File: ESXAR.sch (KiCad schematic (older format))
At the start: 43 parts, among them P1 ANALOG, P10 USB_A, P11 USB_B, P12 SERVO/INPUT, P13 ANALOG, P16 BREADBOARD_POWER, P17 SENSOR, P18 EXTIO, P19 UNIVERSAL, P2 BREADBOARD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

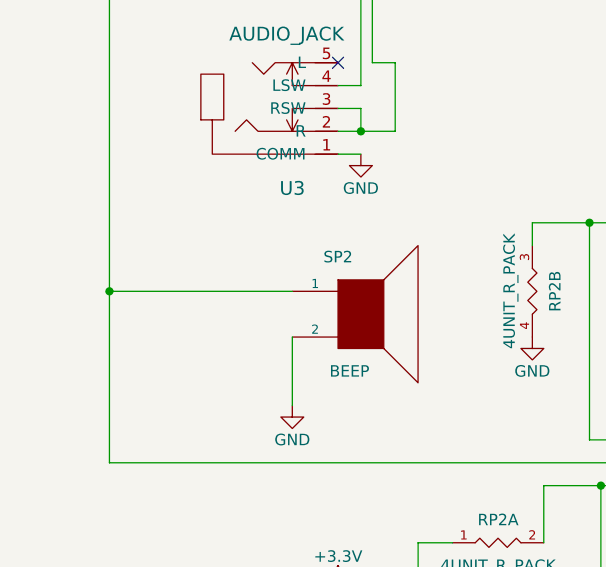
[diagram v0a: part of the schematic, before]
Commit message: Change IO Ext pin direction, and througehwole size.
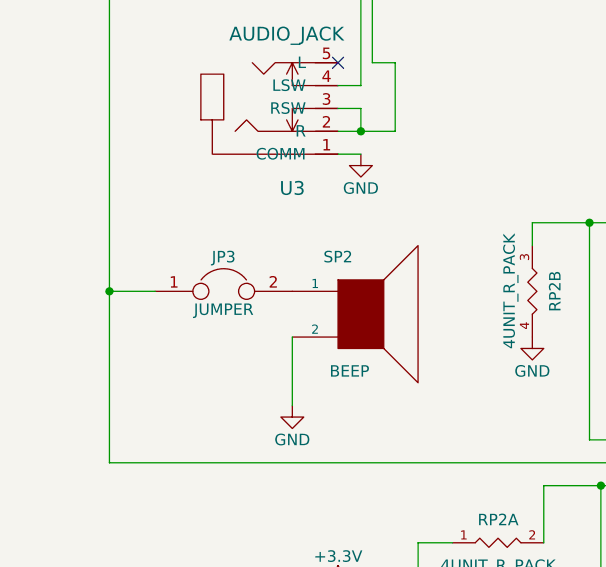
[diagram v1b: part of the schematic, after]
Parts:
- added JP3: JUMPER, symbol JUMPER
- P18, P19, P20: footprint library:SolderWirePad_Oval_9xInline_0-6mmDrill -> library:SolderWirePad_Oval_9xInline_0-7mmDrill
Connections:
- net at P18.7 (P7), P2.7 (P7), P5.7 (P7)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: now also JP3.1; no longer SP2.1
- new net: JP3.2, SP2.1
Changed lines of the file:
@@
 F 0 "P18" H 7900 6200 50  0000 C CNN
 F 1 "EXTIO" H 7900 6300 50  0000 C CNN
-F 2 "library:SolderWirePad_Oval_9xInline_0-6mmDrill" H 7900 5700 50  0001 C CNN
+F 2 "library:SolderWirePad_Oval_9xInline_0-7mmDrill" H 7900 5700 50  0001 C CNN
 F 3 "" H 7900 5700 50  0000 C CNN
 	1    7900 5700
@@
 F 0 "P19" H 9350 6200 50  0000 C CNN
 F 1 "UNIVERSAL" H 9350 6300 50  0000 C CNN
-F 2 "library:SolderWirePad_Oval_9xInline_0-6mmDrill" H 9350 5700 50  0001 C CNN
+F 2 "library:SolderWirePad_Oval_9xInline_0-7mmDrill" H 9350 5700 50  0001 C CNN
 F 3 "" H 9350 5700 50  0000 C CNN
 	1    9350 5700
@@
 F 0 "P20" H 9650 6200 50  0000 C CNN
 F 1 "UNIVERSAL" H 9800 6300 50  0000 C CNN
-F 2 "library:SolderWirePad_Oval_9xInline_0-6mmDrill" H 9650 5700 50  0001 C CNN
+F 2 "library:SolderWirePad_Oval_9xInline_0-7mmDrill" H 9650 5700 50  0001 C CNN
 F 3 "" H 9650 5700 50  0000 C CNN
 	1    9650 5700
@@
 Wire Wire Line
 	2200 5250 2200 4950
-Wire Wire Line
-	2200 4750 1400 4750
 Connection ~ 1400 4750
 Wire Wire Line
@@
 Wire Wire Line
 	2550 3750 2650 3750
+$Comp
+L JUMPER JP3
+U 1 1 57A07E84
+P 1900 4750
+F 0 "JP3" H 1900 4900 50  0000 C CNN
+F 1 "JUMPER" H 1900 4670 50  0000 C CNN
+F 2 "" H 1900 4750 50  0001 C CNN
+F 3 "" H 1900 4750 50  0000 C CNN
+	1    1900 4750
+	1    0    0    -1
+$EndComp
+Wire Wire Line
+	1400 4750 1600 4750
 $EndSCHEMATC

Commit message: fix registor array bug
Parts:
- RP2: footprint Resistors_SMD:R_Array_Convex_4x1206 -> library:R_Array_For_R_Multi_library_4x1206
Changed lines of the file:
@@
 F 0 "RP2" H 3250 4850 50  0000 C CNN
 F 1 "4UNIT_R_PACK" H 3250 4650 50  0000 C CNN
-F 2 "Resistors_SMD:R_Array_Convex_4x1206" H 3200 4650 50  0001 C CNN
+F 2 "library:R_Array_For_R_Multi_library_4x1206" H 3200 4650 50  0001 C CNN
 F 3 "" H 3200 4650 50  0000 C CNN
 	2    3250 4750
@@
 F 0 "RP2" H 3850 3700 50  0000 C CNN
 F 1 "4UNIT_R_PACK" H 3850 3500 50  0000 C CNN
-F 2 "Resistors_SMD:R_Array_Convex_4x1206" H 3800 3500 50  0001 C CNN
+F 2 "library:R_Array_For_R_Multi_library_4x1206" H 3800 3500 50  0001 C CNN
 F 3 "" H 3800 3500 50  0000 C CNN
 	3    3850 3600
@@
 F 0 "RP2" H 3100 5950 50  0000 C CNN
 F 1 "4UNIT_R_PACK" H 3100 5750 50  0000 C CNN
-F 2 "Resistors_SMD:R_Array_Convex_4x1206" H 3050 5750 50  0001 C CNN
+F 2 "library:R_Array_For_R_Multi_library_4x1206" H 3050 5750 50  0001 C CNN
 F 3 "" H 3050 5750 50  0000 C CNN
 	1    3100 5850
@@
 F 0 "RP2" H 6150 3550 50  0000 C CNN
 F 1 "4UNIT_R_PACK" H 6150 3350 50  0000 C CNN
-F 2 "Resistors_SMD:R_Array_Convex_4x1206" H 6100 3350 50  0001 C CNN
+F 2 "library:R_Array_For_R_Multi_library_4x1206" H 6100 3350 50  0001 C CNN
 F 3 "" H 6100 3350 50  0000 C CNN
 	4    6150 3450

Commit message: Ver 20160802. add speaker jumper,change analog port layout, etc.
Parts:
- added R1: 4.7kΩ, Resistors_SMD:R_1206, symbol R
- JP3: footprint (none) -> Pin_Headers:Pin_Header_Straight_1x02
- U5: footprint Housings_DIP:DIP-4_W7.62mm -> Opto-Devices:Optocoupler_SMD_HandSoldering_KPC357_LTV35x_PC357_SingleChannel
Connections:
- net GND: now also R1.1
- net at P13.1 (P1), P17.2 (P2), P8.2 (P2)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: now also R1.2
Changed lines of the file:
@@
 F 0 "U5" H 7150 2900 50  0000 L CNN
 F 1 "TLP222A" H 7350 2900 50  0000 L CNN
-F 2 "Housings_DIP:DIP-4_W7.62mm" H 7150 2500 50  0000 L CIN
+F 2 "Opto-Devices:Optocoupler_SMD_HandSoldering_KPC357_LTV35x_PC357_SingleChannel" H 7150 2500 50  0000 L CIN
 F 3 "" H 7300 2700 50  0000 L CNN
 	1    7350 2700
@@
 	5150 3300 5150 3150
 Wire Wire Line
-	4900 3300 5150 3300
+	4750 3300 5150 3300
 Wire Wire Line
 	4900 3250 4900 3300
@@
 F 0 "JP3" H 1900 4900 50  0000 C CNN
 F 1 "JUMPER" H 1900 4670 50  0000 C CNN
-F 2 "" H 1900 4750 50  0001 C CNN
+F 2 "Pin_Headers:Pin_Header_Straight_1x02" H 1900 4750 50  0001 C CNN
 F 3 "" H 1900 4750 50  0000 C CNN
 	1    1900 4750
@@
 Wire Wire Line
 	1400 4750 1600 4750
+$Comp
+L R R1
+U 1 1 57A07626
+P 4750 3100
+F 0 "R1" V 4830 3100 50  0000 C CNN
+F 1 "4.7kΩ" V 4750 3100 50  0000 C CNN
+F 2 "Resistors_SMD:R_1206" V 4680 3100 50  0001 C CNN
+F 3 "" H 4750 3100 50  0000 C CNN
+	1    4750 3100
+	-1   0    0    1
+$EndComp
+Wire Wire Line
+	4750 3250 4750 3300
+Connection ~ 4900 3300
+Connection ~ 4750 2950
 $EndSCHEMATC

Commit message: Ver 20160804 Layout Change.
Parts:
- added C5, C8: 100uF, Capacitors_ThroughHole:C_Radial_D6.3_L11.2_P2.5, symbol CP
- added C6, C7: 10uF, library:C_1206_HandSoldering_Small, symbol C
- added L1: 4.7uH, library:C_1206_HandSoldering_Small, symbol INDUCTOR_SMALL
- added SW2: DIN, Buttons_Switches_ThroughHole:SW_PUSH_SMALL, symbol SW_PUSH
- added U4: MT5201-3.3N, TO_SOT_Packages_SMD:SOT-23-5, symbol MT5201-3.3N
- added U7: LD1117CV33, Power_Integrations:TO-220, symbol LT1129MPST-3.3
- added U8: TA48M033F, TO_SOT_Packages_THT:SOT126_SOT32_Housing_Vertical_Mirrored, symbol LT1129MPST-3.3
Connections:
- net +3V3: now also C7.1, C8.1, L1.2, U4.5 (VOUT), U7.3 (OUT), U8.3 (OUT)
- net +5V: now also C5.1, C6.1, U4.1 (EN), U4.4 (VIN), U7.1 (VIN), U8.1 (VIN)
- net GND: now also C5.2, C6.2, C7.2, C8.2, SW2.2, U4.2 (GND), U7.2 (GND), U8.2 (GND)
- net at P12.1 (P1), P18.2 (P2), P2.2 (P2)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: now also SW2.1
- new net: L1.1, U4.3 (SW)
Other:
- moved on the sheet: U6

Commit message: Ver.20170816  and documents
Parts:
- removed C4: 0.1uF, Capacitors_ThroughHole:C_Disc_D3_P2.5, symbol C
- removed R10, R11, R6, R7, R8, R9: 4.7kΩ, Discret:R1, symbol R
- removed U2: NJM4556A, Housings_DIP:DIP-8_W7.62mm, symbol LM358N
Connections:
- net at JP3.1, P18.7 (P7), P2.7 (P7)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: now also JP3.2, SP2.1
- net at C3.1: now also P4.1 (P1)
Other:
- moved on the sheet: JP3, P4
